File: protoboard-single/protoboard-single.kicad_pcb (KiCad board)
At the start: 2 copper layers, 38.1 x 27.9 mm, 1 part, among them J1 MODULE_HEADER

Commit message: mvp
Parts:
- added J10: MODULE_HEADER, parts:1x10, F.Cu at (154.9, 101.6)
- added J11: MODULE_HEADER, parts:1x10, F.Cu at (157.5, 101.6)
- added J12: MODULE_HEADER, parts:1x10, F.Cu at (160.0, 101.6)
- added J13: MODULE_HEADER, parts:1x10, F.Cu at (162.6, 101.6)
- added J14: MODULE_HEADER, parts:1x10, F.Cu at (132.1, 101.6)
- added J2: MODULE_HEADER, parts:1x10, F.Cu at (134.6, 101.6)
- added J3: MODULE_HEADER, parts:1x10, F.Cu at (137.2, 101.6)
- added J4: MODULE_HEADER, parts:1x10, F.Cu at (139.7, 101.6)
- added J5: MODULE_HEADER, parts:1x10, F.Cu at (142.2, 101.6)
- added J6: MODULE_HEADER, parts:1x10, F.Cu at (144.8, 101.6)
- added J7: MODULE_HEADER, parts:1x10, F.Cu at (147.3, 101.6)
- added J8: MODULE_HEADER, parts:1x10, F.Cu at (149.9, 101.6)
- added J9: MODULE_HEADER, parts:1x10, F.Cu at (152.4, 101.6)
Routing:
- net Net-(J1-Pad2): track 0.00 -> 122.1 mm
- net Net-(J1-Pad1): track 0.00 -> 64.4 mm
- net Net-(J1-Pad9): track 0.00 -> 3.18 mm
- net Net-(J1-Pad8): track 0.00 -> 3.18 mm
- net Net-(J1-Pad7): track 0.00 -> 3.18 mm
- net Net-(J1-Pad6): track 0.00 -> 3.18 mm
- net Net-(J1-Pad5): track 0.00 -> 3.18 mm
- net Net-(J1-Pad4): track 0.00 -> 3.18 mm
- net Net-(J1-Pad3): track 0.00 -> 3.18 mm
- net Net-(J1-Pad10): track 0.00 -> 3.18 mm
- net (no net): vias 0 -> 10
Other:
- net class Default: via_dia 0.889 -> 1.524; via_drill 0.635 -> 0.889
- rule via_min_drill: 0.508 -> 0.889
- rule via_min_size: 0.889 -> 1.524
- board text added: "3.3V"
- board text added: "DIY"
- board text added: "GND"

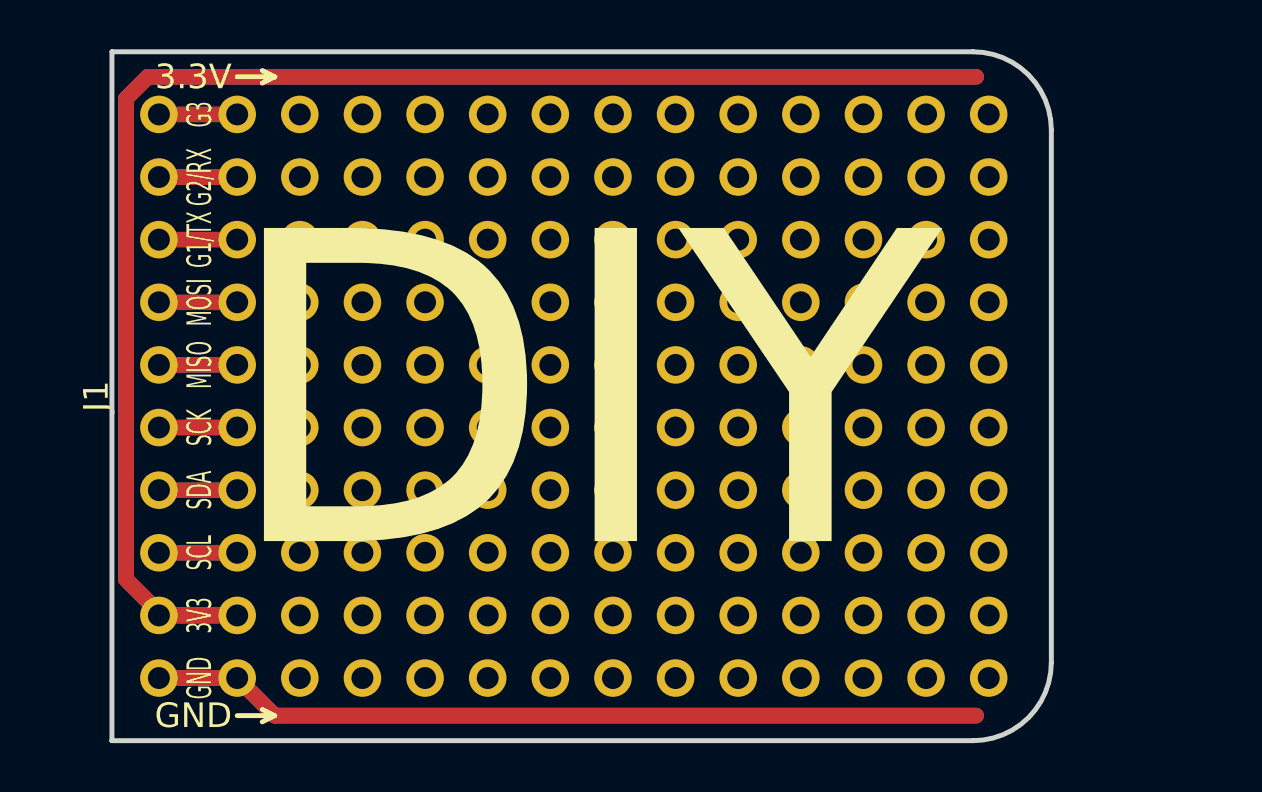
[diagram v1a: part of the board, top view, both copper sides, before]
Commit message: more access to each signal
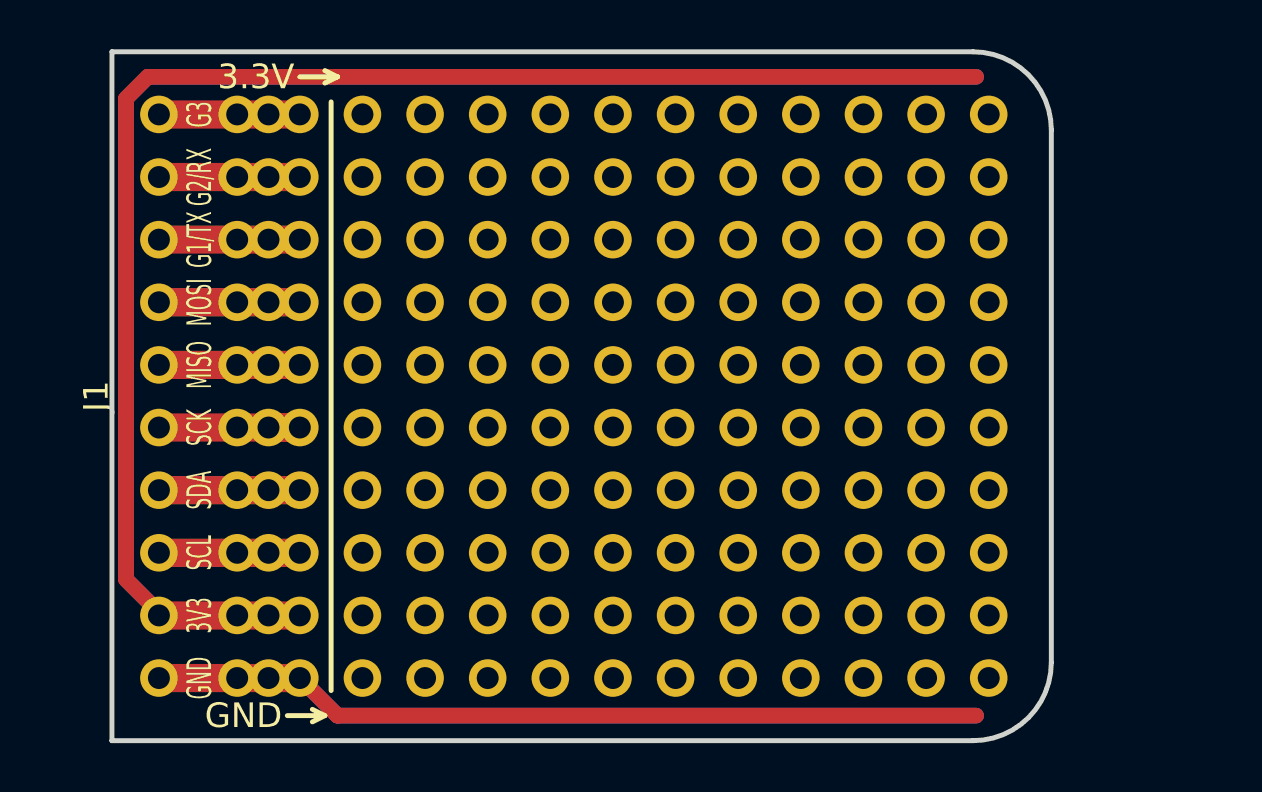
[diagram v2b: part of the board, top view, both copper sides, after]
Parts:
- added J15: MODULE_HEADER, parts:1x10, F.Cu at (133.3, 101.6)
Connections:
- J2 pad 1: Net-(J2-Pad1) -> Net-(J1-Pad1)
- J2 pad 10: Net-(J2-Pad10) -> Net-(J1-Pad10)
- J2 pad 2: Net-(J2-Pad2) -> Net-(J1-Pad2)
- J2 pad 3: Net-(J2-Pad3) -> Net-(J1-Pad3)
- J2 pad 4: Net-(J2-Pad4) -> Net-(J1-Pad4)
- J2 pad 5: Net-(J2-Pad5) -> Net-(J1-Pad5)
- J2 pad 6: Net-(J2-Pad6) -> Net-(J1-Pad6)
- J2 pad 7: Net-(J2-Pad7) -> Net-(J1-Pad7)
- J2 pad 8: Net-(J2-Pad8) -> Net-(J1-Pad8)
- J2 pad 9: Net-(J2-Pad9) -> Net-(J1-Pad9)
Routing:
- net Net-(J1-Pad5): track 3.18 -> 6.99 mm
- net Net-(J1-Pad9): track 3.18 -> 5.72 mm
- net Net-(J1-Pad8): track 3.18 -> 5.72 mm
- net Net-(J1-Pad7): track 3.18 -> 5.72 mm
- net Net-(J1-Pad6): track 3.18 -> 5.72 mm
- net Net-(J1-Pad4): track 3.18 -> 5.72 mm
- net Net-(J1-Pad3): track 3.18 -> 5.72 mm
- net Net-(J1-Pad2): track 122.1 -> 124.6 mm
- net Net-(J1-Pad10): track 3.18 -> 5.72 mm
- net Net-(J1-Pad1): track 64.4 -> 66.9 mm
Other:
- board text removed: "DIY"

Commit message: ship it
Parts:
- added SILK1: logo, parts:TESSEL-HEXAGON-LOGO, F.Cu at (148.6, 100.8)
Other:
- board text added: "DIY"
